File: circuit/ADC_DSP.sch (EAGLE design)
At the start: 70 parts, among them IC1 REG1117, IC3 STM32F40XRXT6, IC4 CS4272, Q1 8MHz, Q2 24.576MHz

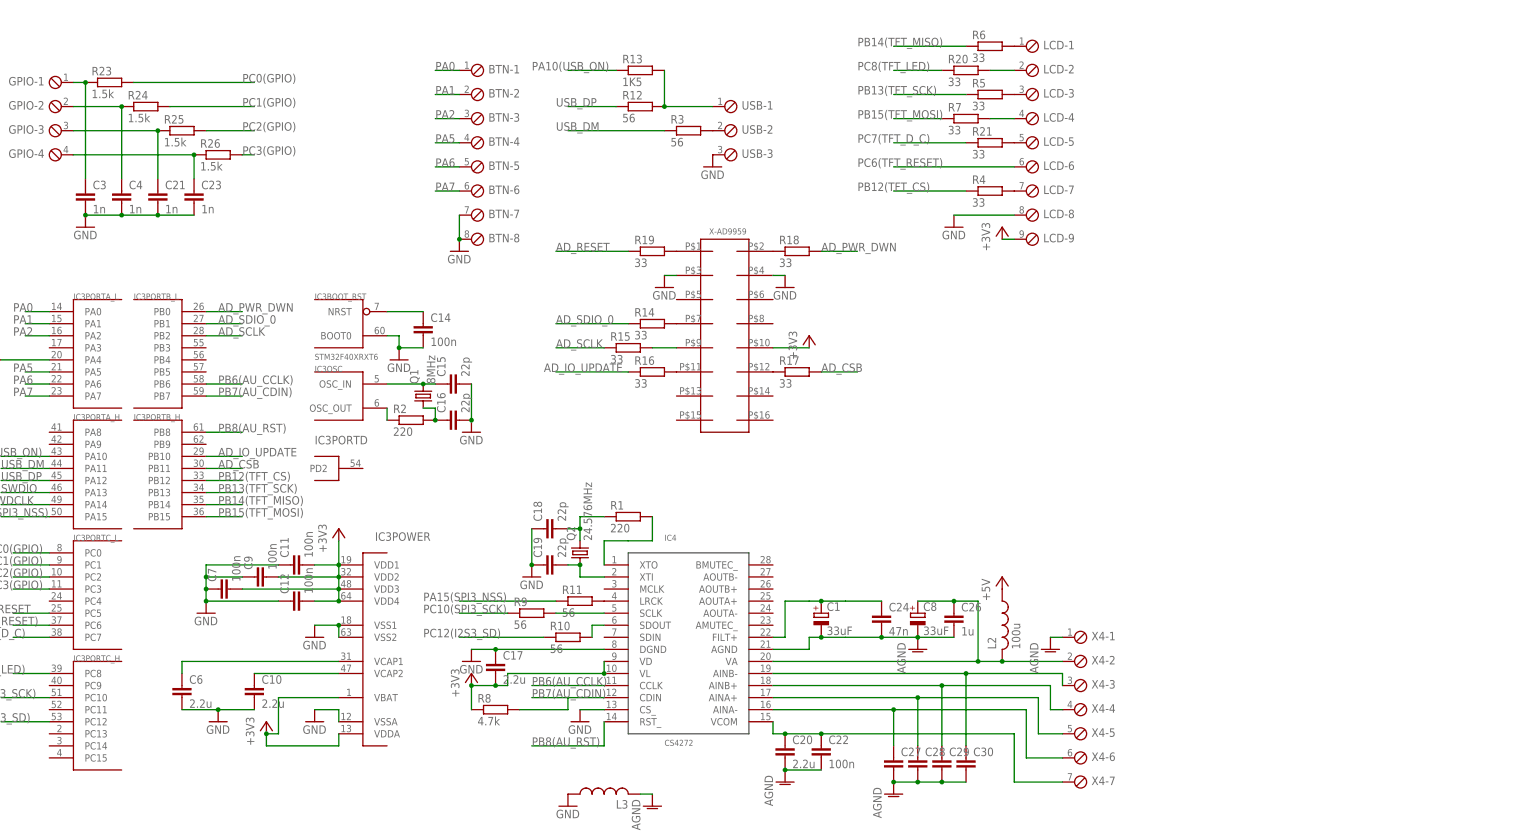
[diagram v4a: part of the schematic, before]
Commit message: - развели вход для CS4272
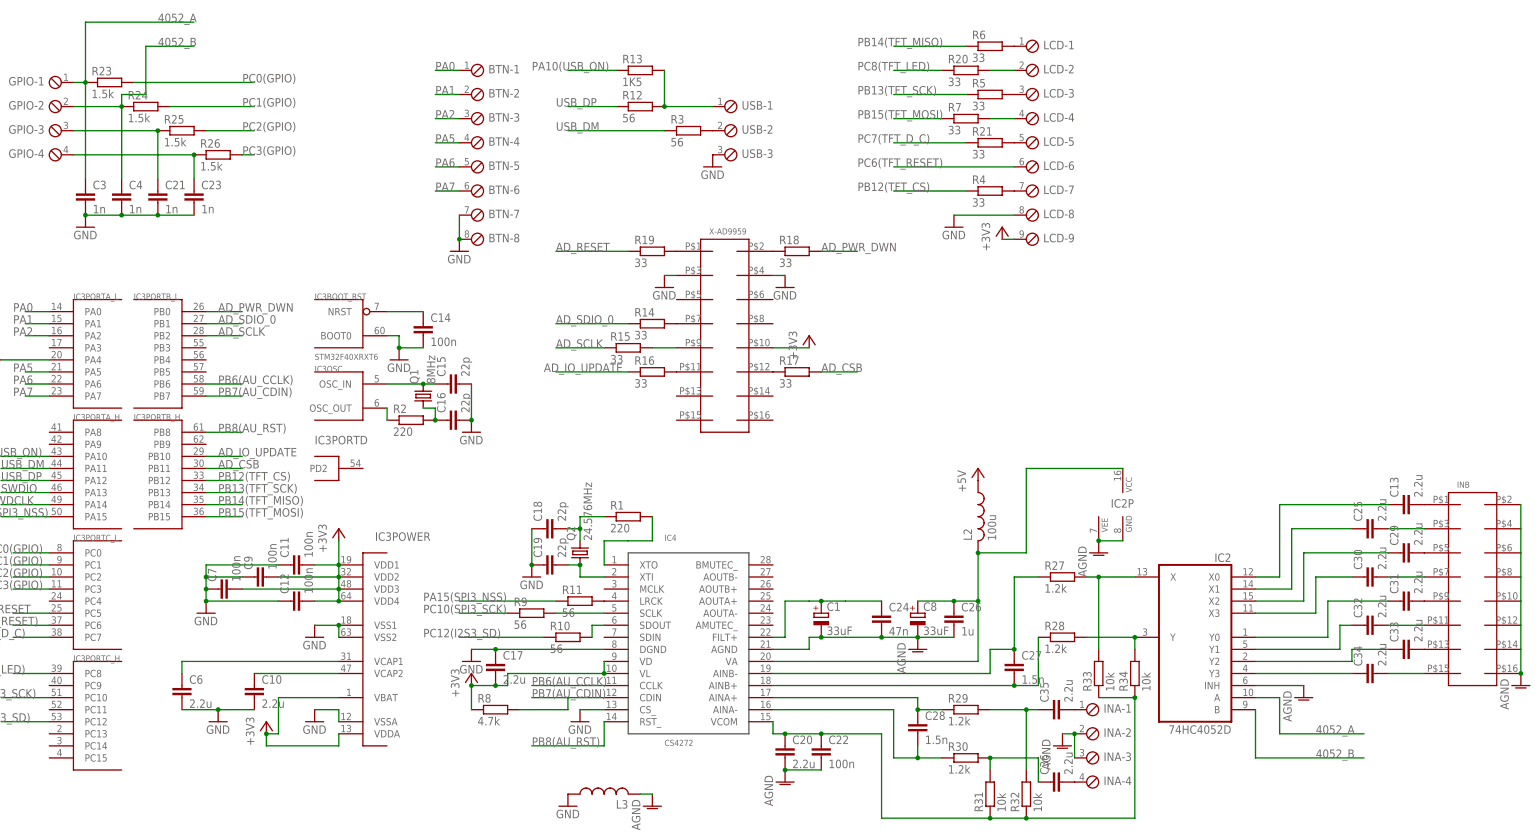
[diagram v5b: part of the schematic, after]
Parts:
- removed X4: (no value), con-phoenix-254:MPT7
- added C13, C25, C31, C32, C33, C34, C35, C36: 2.2u, rcl:C-EUC0603
- added IC2: 74HC4052D, 40xx:4052D
- added INA: (no value), con-phoenix-254:MPT4
- added INB: PIN8X2, balmer:PIN8X2
- added R27, R28, R29, R30: 1.2k, rcl:R-EU_R0603
- added R31, R32, R33, R34: 10k, rcl:R-EU_R0603
- C27, C28: value (none) -> 1.5n
- C29, C30: value (none) -> 2.2u; device rcl:C-EUC0805 -> rcl:C-EUC0603
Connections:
- removed net AINA+: C28.1, IC4.AINA+, X4-5.1
- removed net N$38: C3.1, GPIO-1.1, R23.1
- removed net N$39: C4.1, GPIO-2.1, R24.1
- new net 4052_A: C3.1, GPIO-1.1, IC2A.A, R23.1
- new net 4052_B: C4.1, GPIO-2.1, IC2A.B, R24.1
- new net N$13: C13.2, INB.P$1
- new net N$26: C34.2, INB.P$15
- new net N$28: C32.1, IC2A.Y1
- new net N$30: C31.1, IC2A.Y0
- new net N$42: C30.1, IC2A.X3
- new net N$43: C29.1, IC2A.X2
- new net N$44: C25.1, IC2A.X1
- new net N$45: C13.1, IC2A.X0
- new net N$46: IC2A.X, R27.2, R33.2
- new net N$47: IC2A.Y, R28.2, R34.2
- new net N$48: C28.2, IC4.AINA-, R30.1
- new net N$49: C25.2, INB.P$3
- new net N$50: C35.1, R29.2, R32.2
- new net N$51: C36.1, R30.2, R31.2
- new net N$52: C29.2, INB.P$5
- new net N$53: C31.2, INB.P$9
- new net N$54: C33.2, INB.P$13
- new net N$55: C34.1, IC2A.Y3
- new net N$56: C33.1, IC2A.Y2
- new net N$57: C32.2, INB.P$11
- new net N$58: C30.2, INB.P$7
- new net N$59: C35.2, INA-1.1
- new net N$60: C36.2, INA-4.1
- net AGND: now also IC2A.INH, IC2P.GND, IC2P.VEE, INA-2.1, INA-3.1, INB.P$10, INB.P$12, INB.P$14, INB.P$16, INB.P$2, INB.P$4, INB.P$6, INB.P$8; no longer C27.2, C28.2, C29.2, C30.2, X4-1.1
- net AINB+: now also C27.2, R28.1; no longer C29.1, X4-4.1
- net AVCC: now also IC2P.VCC; no longer X4-2.1
- net N$15: now also C27.1, R27.1; no longer C30.1, X4-3.1
- net N$18: now also C28.1, IC4.AINA+, R29.1; no longer C27.1, IC4.AINA-, X4-6.1
- net VCOM: now also R31.1, R32.1, R33.1, R34.1; no longer X4-7.1
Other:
- moved on the sheet: C27, C28, C29, C30, L2

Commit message: - перед заменой на более быстрый мультиплексор.
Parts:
- removed C29, C30, C31, C32, C33, C34: 2.2u, rcl:C-EUC0603
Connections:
- removed net N$49: C25.2, INB.P$3
- removed net N$52: C29.2, INB.P$5
- removed net N$53: C31.2, INB.P$9
- removed net N$54: C33.2, INB.P$13
- removed net N$55: C34.1, IC2A.Y3
- removed net N$56: C33.1, IC2A.Y2
- removed net N$57: C32.2, INB.P$11
- removed net N$58: C30.2, INB.P$7
- new net N$38: IC2A.Y2, INB.P$13
- new net N$39: C25.1, R28.2, R34.2
- net N$13: now also C25.2, IC2A.Y; no longer C13.2, INB.P$1
- net N$26: now also IC2A.Y3; no longer C34.2
- net N$28: now also C13.1, R27.2, R33.2; no longer C32.1, IC2A.Y1
- net N$30: now also C13.2, IC2A.X; no longer C31.1, IC2A.Y0
- net N$42: now also IC2A.Y1, INB.P$11; no longer C30.1, IC2A.X3
- net N$43: now also IC2A.Y0, INB.P$9; no longer C29.1, IC2A.X2
- net N$44: now also IC2A.X3, INB.P$7; no longer C25.1, IC2A.X1
- net N$45: now also IC2A.X2, INB.P$5; no longer C13.1, IC2A.X0
- net N$46: now also IC2A.X1, INB.P$3; no longer IC2A.X, R27.2, R33.2
- net N$47: now also IC2A.X0, INB.P$1; no longer IC2A.Y, R28.2, R34.2
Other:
- moved on the sheet: C13, C25, IC2

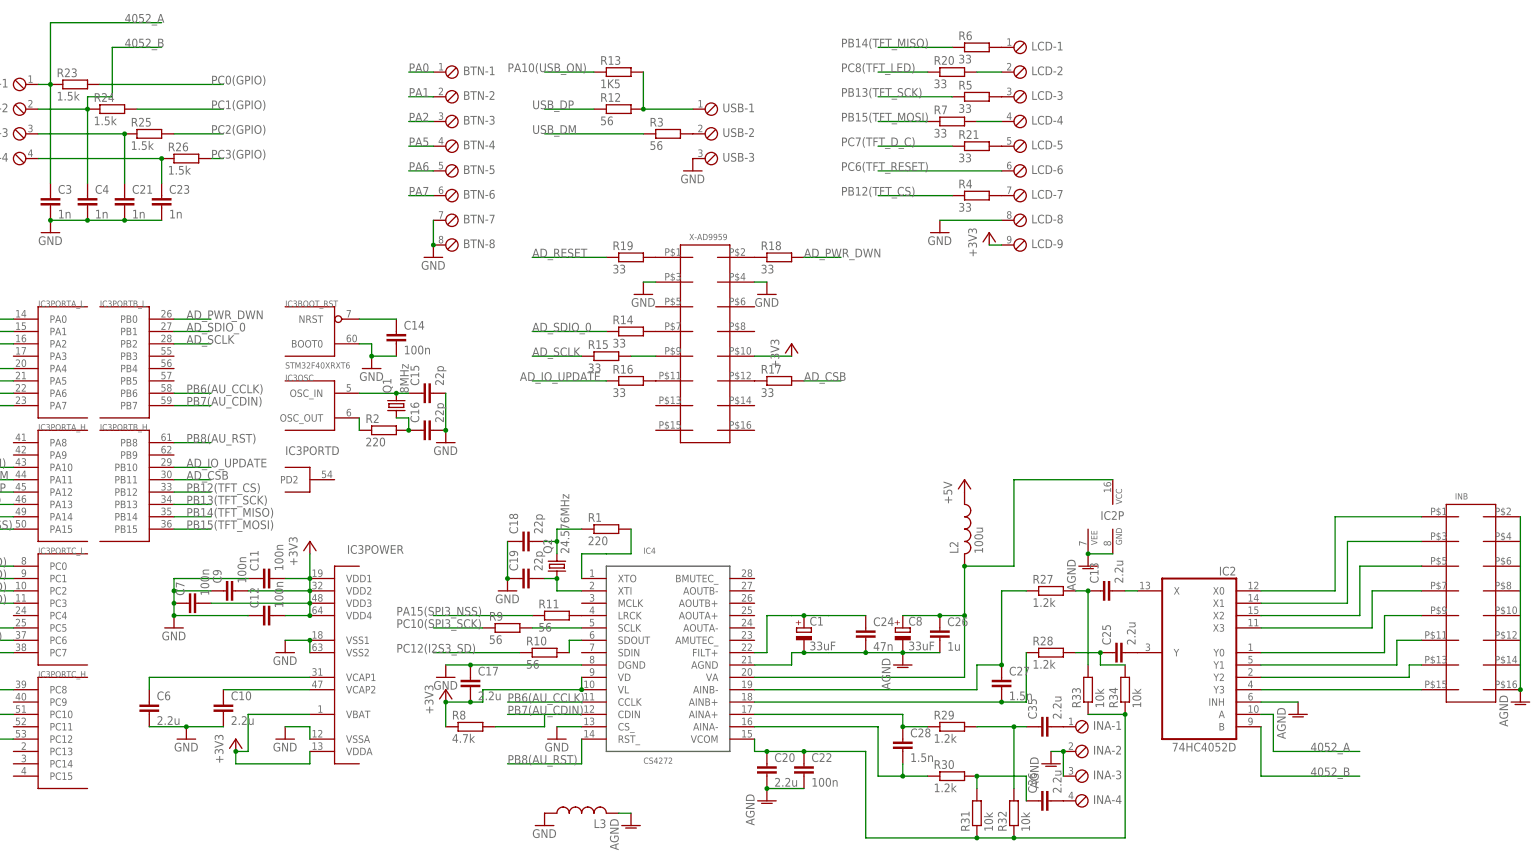
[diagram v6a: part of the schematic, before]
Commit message: - перержавел по халявному под SN74LVC1G3157DBVR
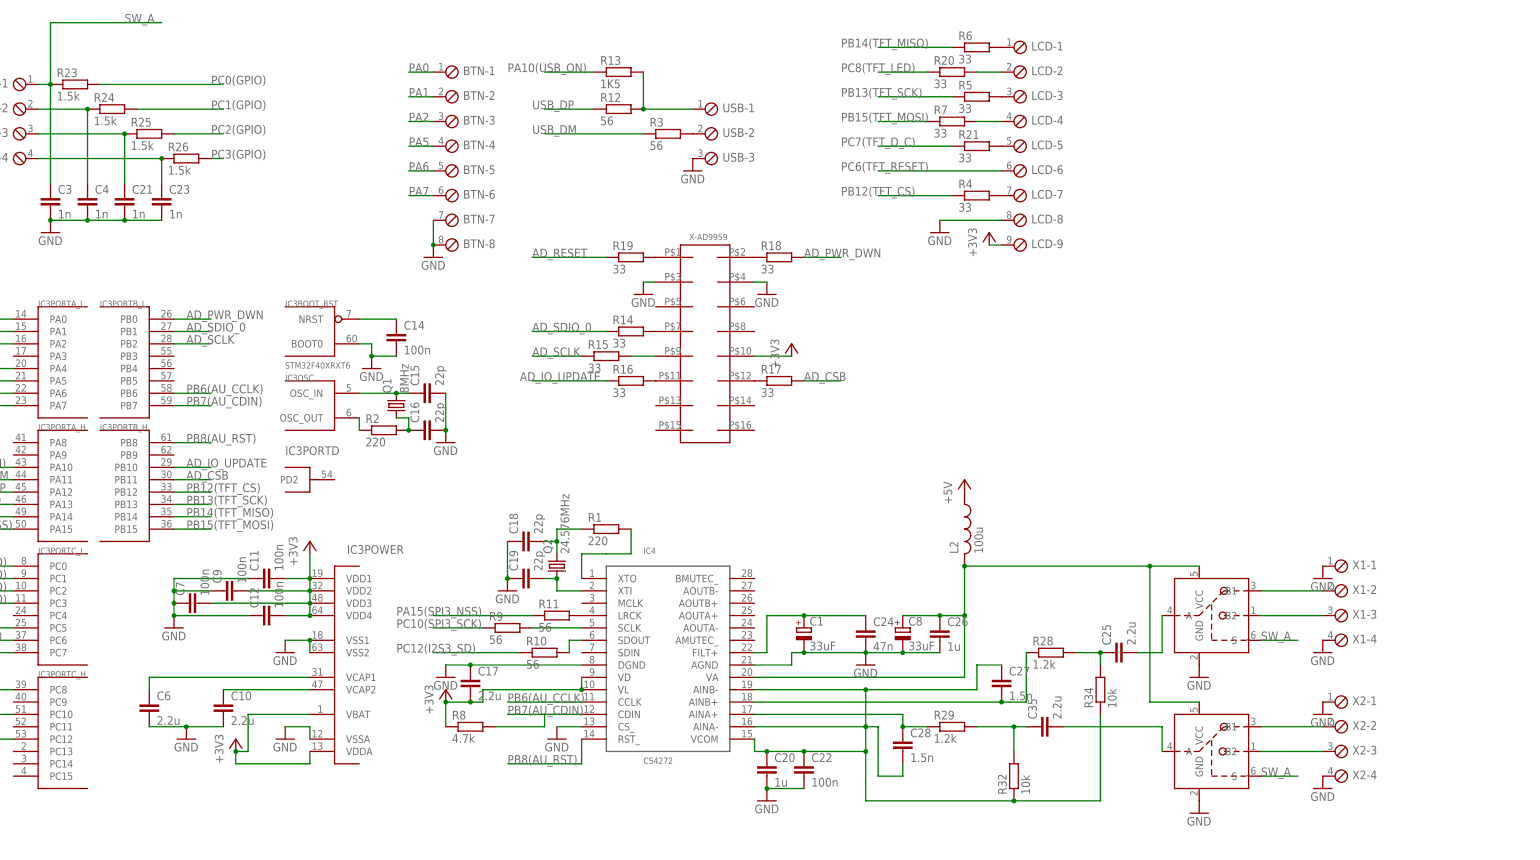
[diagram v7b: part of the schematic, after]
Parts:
- removed C13, C36: 2.2u, rcl:C-EUC0603
- removed IC2: 74HC4052D, 40xx:4052D
- removed INA: (no value), con-phoenix-254:MPT4
- removed INB: PIN8X2, balmer:PIN8X2
- removed L3: (no value), rcl:L-USL2012C
- removed R27, R30: 1.2k, rcl:R-EU_R0603
- removed R31, R33: 10k, rcl:R-EU_R0603
- added U$1, U$2: SN74LVC1G3157DBVR, balmer:SN74LVC1G3157DBVR
- added X1, X2: (no value), con-phoenix-254:MPT4
- C20: value 2.2u -> 1u
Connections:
- removed net 4052_A: C3.1, GPIO-1.1, IC2A.A, R23.1
- removed net AGND: C1.-, C20.2, C22.2, C24.2, C26.2, C8.-, IC2A.INH, IC2P.GND, IC2P.VEE, IC4.AGND, INA-2.1, INA-3.1, INB.P$10, INB.P$12, INB.P$14, INB.P$16, INB.P$2, INB.P$4, INB.P$6, INB.P$8, L3.2
- removed net N$42: IC2A.Y1, INB.P$11
- removed net N$43: IC2A.Y0, INB.P$9
- removed net N$44: IC2A.X3, INB.P$7
- removed net N$45: IC2A.X2, INB.P$5
- removed net N$46: IC2A.X1, INB.P$3
- removed net N$47: IC2A.X0, INB.P$1
- removed net N$48: C28.2, IC4.AINA-, R30.1
- removed net N$51: C36.1, R30.2, R31.2
- removed net N$59: C35.2, INA-1.1
- removed net N$60: C36.2, INA-4.1
- new net SW_A: C3.1, GPIO-1.1, R23.1, U$1.S, U$2.S
- net 4052_B: no longer IC2A.B
- net AVCC: now also U$1.VCC, U$2.VCC; no longer IC2P.VCC
- net GND: now also C1.-, C20.2, C22.2, C24.2, C26.2, C8.-, IC4.AGND, U$1.GND, U$2.GND, X1-1.1, X1-4.1, X2-1.1, X2-4.1; no longer L3.1
- net N$13: now also U$1.A; no longer IC2A.Y
- net N$15: now also C35.2, U$2.A; no longer C27.1, IC4.AINB-, R27.1
- net N$26: now also U$1.B1, X1-2.1; no longer IC2A.Y3, INB.P$15
- net N$28: now also U$1.B2, X1-3.1; no longer C13.1, R27.2, R33.2
- net N$30: now also U$2.B1, X2-2.1; no longer C13.2, IC2A.X
- net N$38: now also U$2.B2, X2-3.1; no longer IC2A.Y2, INB.P$13
- net VCOM: now also C27.1, C28.2, IC4.AINA-, IC4.AINB-; no longer R31.1, R33.1
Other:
- moved on the sheet: R32, R34

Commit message: - более -менее разведенная плата
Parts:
- removed X2: (no value), con-phoenix-254:MPT4
- added C13: 100n, rcl:C-EUC0603
- X1: device con-phoenix-254:MPT4 -> con-phoenix-254:MPT8
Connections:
- net AVCC: now also C13.1
- net GND: now also C13.2, X1-5.1, X1-8.1; no longer X2-1.1, X2-4.1
- net N$30: now also X1-6.1; no longer X2-2.1
- net N$38: now also X1-7.1; no longer X2-3.1
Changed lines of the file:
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@@
 <part name="U$1" library="balmer" deviceset="SN74LVC1G3157DBVR" device=""/>
 <part name="U$2" library="balmer" deviceset="SN74LVC1G3157DBVR" device=""/>
-<part name="X1" library="con-phoenix-254" deviceset="MPT4" device=""/>
-<part name="X2" library="con-phoenix-254" deviceset="MPT4" device=""/>
 <part name="GND13" library="supply1" deviceset="GND" device=""/>
 <part name="GND22" library="supply1" deviceset="GND" device=""/>
@@
 <part name="GND26" library="supply1" deviceset="GND" device=""/>
 <part name="GND27" library="supply1" deviceset="GND" device=""/>
+<part name="X1" library="con-phoenix-254" deviceset="MPT8" device=""/>
+<part name="C13" library="rcl" deviceset="C-EU" device="C0603" value="100n"/>
+<part name="GND28" library="supply1" deviceset="GND" device=""/>
 </parts>
 <sheets>
@@
 <instance part="U$1" gate="G$1" x="271.78" y="15.24"/>
 <instance part="U$2" gate="G$1" x="271.78" y="-12.7"/>
-<instance part="X1" gate="-1" x="297.18" y="25.4"/>
-<instance part="X1" gate="-2" x="297.18" y="20.32"/>
-<instance part="X1" gate="-3" x="297.18" y="15.24"/>
-<instance part="X1" gate="-4" x="297.18" y="10.16"/>
-<instance part="X2" gate="-1" x="297.18" y="-2.54"/>
-<instance part="X2" gate="-2" x="297.18" y="-7.62"/>
-<instance part="X2" gate="-3" x="297.18" y="-12.7"/>
-<instance part="X2" gate="-4" x="297.18" y="-17.78"/>
 <instance part="GND13" gate="1" x="200.66" y="5.08"/>
 <instance part="GND22" gate="1" x="269.24" y="-25.4"/>
@@
 <instance part="GND26" gate="1" x="294.64" y="7.62"/>
 <instance part="GND27" gate="1" x="294.64" y="22.86"/>
+<instance part="X1" gate="-1" x="297.18" y="25.4"/>
+<instance part="X1" gate="-2" x="297.18" y="20.32"/>
+<instance part="X1" gate="-3" x="297.18" y="15.24"/>
+<instance part="X1" gate="-4" x="297.18" y="10.16"/>
+<instance part="X1" gate="-5" x="297.18" y="-2.54"/>
+<instance part="X1" gate="-6" x="297.18" y="-7.62"/>
+<instance part="X1" gate="-7" x="297.18" y="-12.7"/>
+<instance part="X1" gate="-8" x="297.18" y="-17.78"/>
+<instance part="C13" gate="G$1" x="251.46" y="22.86"/>
+<instance part="GND28" gate="1" x="251.46" y="15.24"/>
 </instances>
 <busses>
@@
 </segment>
 <segment>
-<pinref part="X2" gate="-4" pin="1"/>
+<pinref part="GND27" gate="1" pin="GND"/>
+<pinref part="X1" gate="-1" pin="1"/>
+</segment>
+<segment>
+<pinref part="GND26" gate="1" pin="GND"/>
+<pinref part="X1" gate="-4" pin="1"/>
+</segment>
+<segment>
+<pinref part="GND25" gate="1" pin="GND"/>
+<pinref part="X1" gate="-5" pin="1"/>
+</segment>
+<segment>
 <pinref part="GND24" gate="1" pin="GND"/>
-</segment>
-<segment>
-<pinref part="X2" gate="-1" pin="1"/>
-<pinref part="GND25" gate="1" pin="GND"/>
-</segment>
-<segment>
-<pinref part="X1" gate="-4" pin="1"/>
-<pinref part="GND26" gate="1" pin="GND"/>
-</segment>
-<segment>
-<pinref part="X1" gate="-1" pin="1"/>
-<pinref part="GND27" gate="1" pin="GND"/>
+<pinref part="X1" gate="-8" pin="1"/>
+</segment>
+<segment>
+<pinref part="C13" gate="G$1" pin="2"/>
+<pinref part="GND28" gate="1" pin="GND"/>
 </segment>
 </net>
@@
 <wire x1="220.98" y1="25.4" x2="220.98" y2="15.24" width="0.1524" layer="91"/>
 <wire x1="269.24" y1="25.4" x2="259.08" y2="25.4" width="0.1524" layer="91"/>
-<wire x1="259.08" y1="25.4" x2="220.98" y2="25.4" width="0.1524" layer="91"/>
+<wire x1="259.08" y1="25.4" x2="251.46" y2="25.4" width="0.1524" layer="91"/>
 <junction x="220.98" y="25.4"/>
 <pinref part="U$2" gate="G$1" pin="VCC"/>
+<wire x1="251.46" y1="25.4" x2="220.98" y2="25.4" width="0.1524" layer="91"/>
 <wire x1="269.24" y1="-2.54" x2="259.08" y2="-2.54" width="0.1524" layer="91"/>
 <wire x1="259.08" y1="-2.54" x2="259.08" y2="25.4" width="0.1524" layer="91"/>
 <junction x="259.08" y="25.4"/>
+<pinref part="C13" gate="G$1" pin="1"/>
+<junction x="251.46" y="25.4"/>
 </segment>
 </net>
@@
 <segment>
 <pinref part="U$1" gate="G$1" pin="B1"/>
+<wire x1="281.94" y1="20.32" x2="294.64" y2="20.32" width="0.1524" layer="91"/>
 <pinref part="X1" gate="-2" pin="1"/>
-<wire x1="281.94" y1="20.32" x2="294.64" y2="20.32" width="0.1524" layer="91"/>
 </segment>
 </net>
@@
 <segment>
 <pinref part="U$1" gate="G$1" pin="B2"/>
+<wire x1="281.94" y1="15.24" x2="294.64" y2="15.24" width="0.1524" layer="91"/>
 <pinref part="X1" gate="-3" pin="1"/>
-<wire x1="281.94" y1="15.24" x2="294.64" y2="15.24" width="0.1524" layer="91"/>
 </segment>
 </net>
@@
 <segment>
 <pinref part="U$2" gate="G$1" pin="B1"/>
-<pinref part="X2" gate="-2" pin="1"/>
 <wire x1="281.94" y1="-7.62" x2="294.64" y2="-7.62" width="0.1524" layer="91"/>
+<pinref part="X1" gate="-6" pin="1"/>
 </segment>
 </net>
@@
 <segment>
 <pinref part="U$2" gate="G$1" pin="B2"/>
-<pinref part="X2" gate="-3" pin="1"/>
 <wire x1="281.94" y1="-12.7" x2="294.64" y2="-12.7" width="0.1524" layer="91"/>
-</segment>
-</net>
+<pinref part="X1" gate="-7" pin="1"/>
+</segment>
+</net>
